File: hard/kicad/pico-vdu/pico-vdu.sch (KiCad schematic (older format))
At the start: 19 parts, among them M3 M3, U1 65C02, U10 74HC21, U11 74HC32, U2 74HC138, U3 74HC245, U4 74HC245, U5 74HC4040, U6 (74HC)4040, U7 6264/62256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

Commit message: some updates on pico-VDU
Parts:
- added U12: 74HC166, Package_DIP:DIP-16_W7.62mm_Socket, symbol 74xx:74LS166
- added U13: 74HC14, Package_DIP:DIP-14_W7.62mm_Socket, symbol 74xx:74HC14
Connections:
- net +5V: now also U12.1 (Ds), U12.16 (VCC), U12.9 (Clr), U13.14 (VCC)
- net DOT: now also U12.7 (Clk)
- net GND: now also U12.6 (CE), U12.8 (GND), U13.7 (GND)
- net VD0: now also U12.2 (A)
- net VD1: now also U12.3 (B)
- net VD2: now also U12.4 (C)
- net VD3: now also U12.5 (D)
- net VD4: now also U12.10 (E)
- net VD5: now also U12.11 (F)
- net VD6: now also U12.12 (G)
- net VD7: now also U12.14 (H)
- net ~CPU: now also U8.19 (CE)
- net ~LOST: now reaches U5.5 (Q3)
- no-connect marks 29 -> 28
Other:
- note added: "$0000-$1FFF\n\n$2000-$3FFF\n\n$4000-$5FFF\n\n$6000-$7FFF"
- moved on the sheet: R1, RN1, RN2, RN3, U11A, U11B, U11C, U11D, U7, U8, U9A

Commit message: remove stand and new tracks on pico-VDU
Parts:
- removed M3: M3, MountingHole:MountingHole_3.2mm_M3_DIN965_Pad, symbol Mechanical:MountingHole_Pad
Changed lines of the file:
@@
-	1    0    0    -1
-$EndComp
-$Comp
-L Mechanical:MountingHole_Pad M3
-U 1 1 663ED7C2
-P 1300 5650
-F 0 "M3" H 1400 5699 50  0000 L CNN
-F 1 "M3" H 1400 5608 50  0000 L CNN
-F 2 "MountingHole:MountingHole_3.2mm_M3_DIN965_Pad" H 1300 5650 50  0001 C CNN
-F 3 "~" H 1300 5650 50  0001 C CNN
-	1    1300 5650
 	1    0    0    -1
 $EndComp
@@
 	700  5750 1000 5750
 Connection ~ 1000 5750
-Wire Wire Line
-	1000 5750 1300 5750
 $Comp
 L power:GND #PWR0117

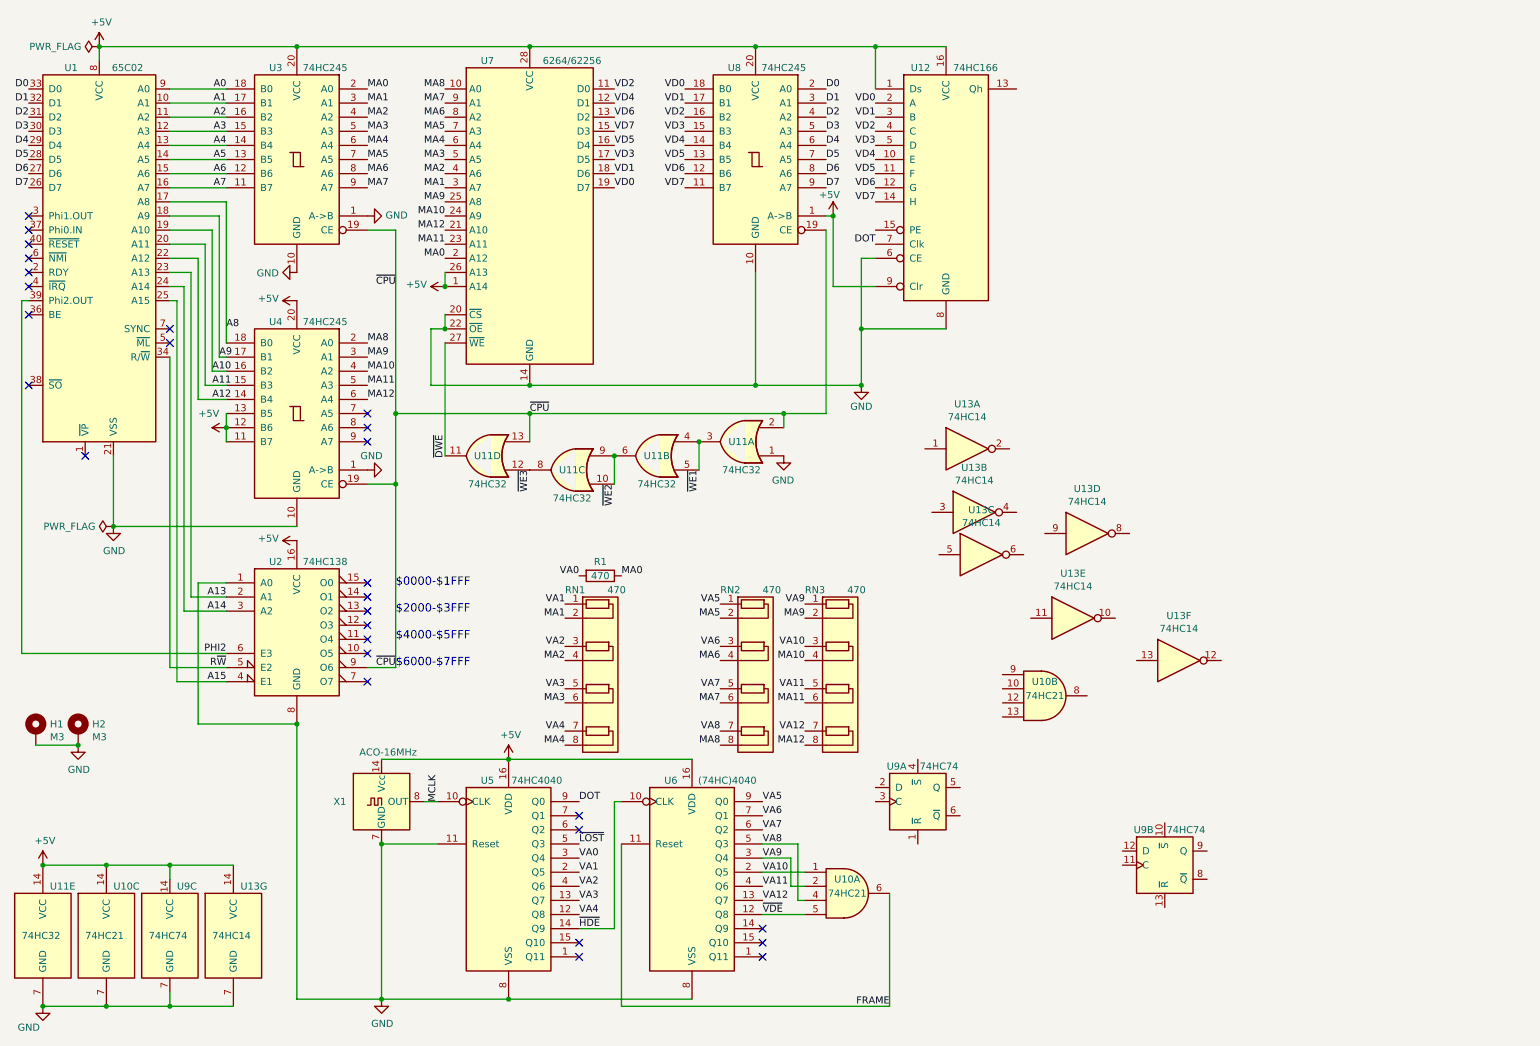
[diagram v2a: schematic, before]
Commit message: all addresses and thicker RCs
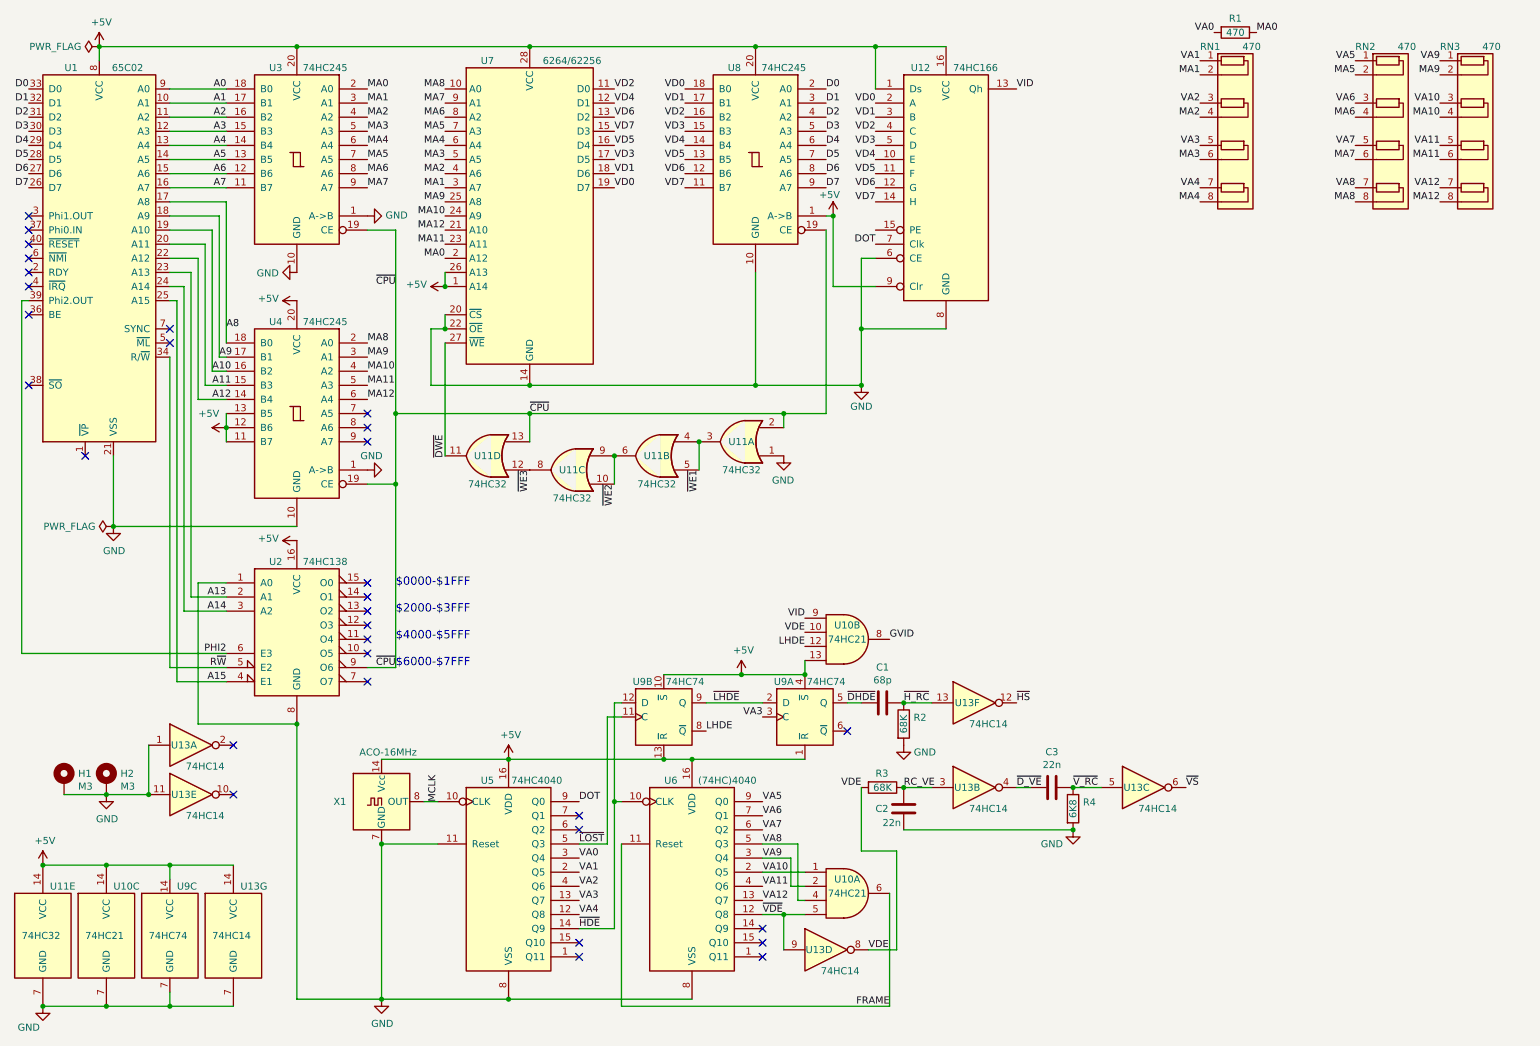
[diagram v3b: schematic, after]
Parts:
- added C1: 68p, Capacitor_THT:C_Disc_D3.8mm_W2.6mm_P2.50mm, symbol Device:C
- added C2, C3: 22n, Capacitor_THT:C_Rect_L7.2mm_W2.5mm_P5.00mm_FKS2_FKP2_MKS2_MKP2, symbol Device:C
- added R2, R3: 68K, Resistor_THT:R_Axial_DIN0207_L6.3mm_D2.5mm_P2.54mm_Vertical, symbol Device:R
- added R4: 6K8, Resistor_THT:R_Axial_DIN0207_L6.3mm_D2.5mm_P2.54mm_Vertical, symbol Device:R
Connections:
- net +5V: now also U10.13, U9.1 (~R), U9.10 (~S), U9.13 (~R), U9.4 (~S)
- net GND: now also U13.1, U13.11, C2.1, R2.2, R4.2
- net VA3: now also U9.3 (C)
- net ~HDE: now also U9.12 (D)
- net ~LOST: now also U9.11 (C)
- net ~VDE: now also U13.9
- net VDE: now reaches U10.10
- net VDE: now also U13.8, R3.2
- net LHDE: now reaches U10.12
- net LHDE: now also U9.8 (~Q)
- net GVID: now reaches U10.8
- net VID: now reaches U10.9
- net VID: now also U12.13 (Qh)
- net ~LHDE: now reaches U9.2 (D)
- net ~LHDE: now also U9.9 (Q)
- net ~DHDE: now reaches U9.5 (Q)
- net ~DHDE: now also C1.2
- net RC_VE: now reaches U13.3
- net RC_VE: now also C2.2, R3.1
- net ~D_VE: now reaches U13.4
- net ~D_VE: now also C3.2
- net ~V_RC: now reaches U13.5
- net ~V_RC: now also C3.1, R4.1
- net ~VS: now reaches U13.6
- net ~HS: now reaches U13.12
- net ~H_RC: now reaches U13.13
- net ~H_RC: now also C1.1, R2.1
- no-connect marks 28 -> 31
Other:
- moved on the sheet: H1, H2, R1, RN1, RN2, RN3, U10B, U13A, U13B, U13C, U13D, U13E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

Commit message: generate shift load
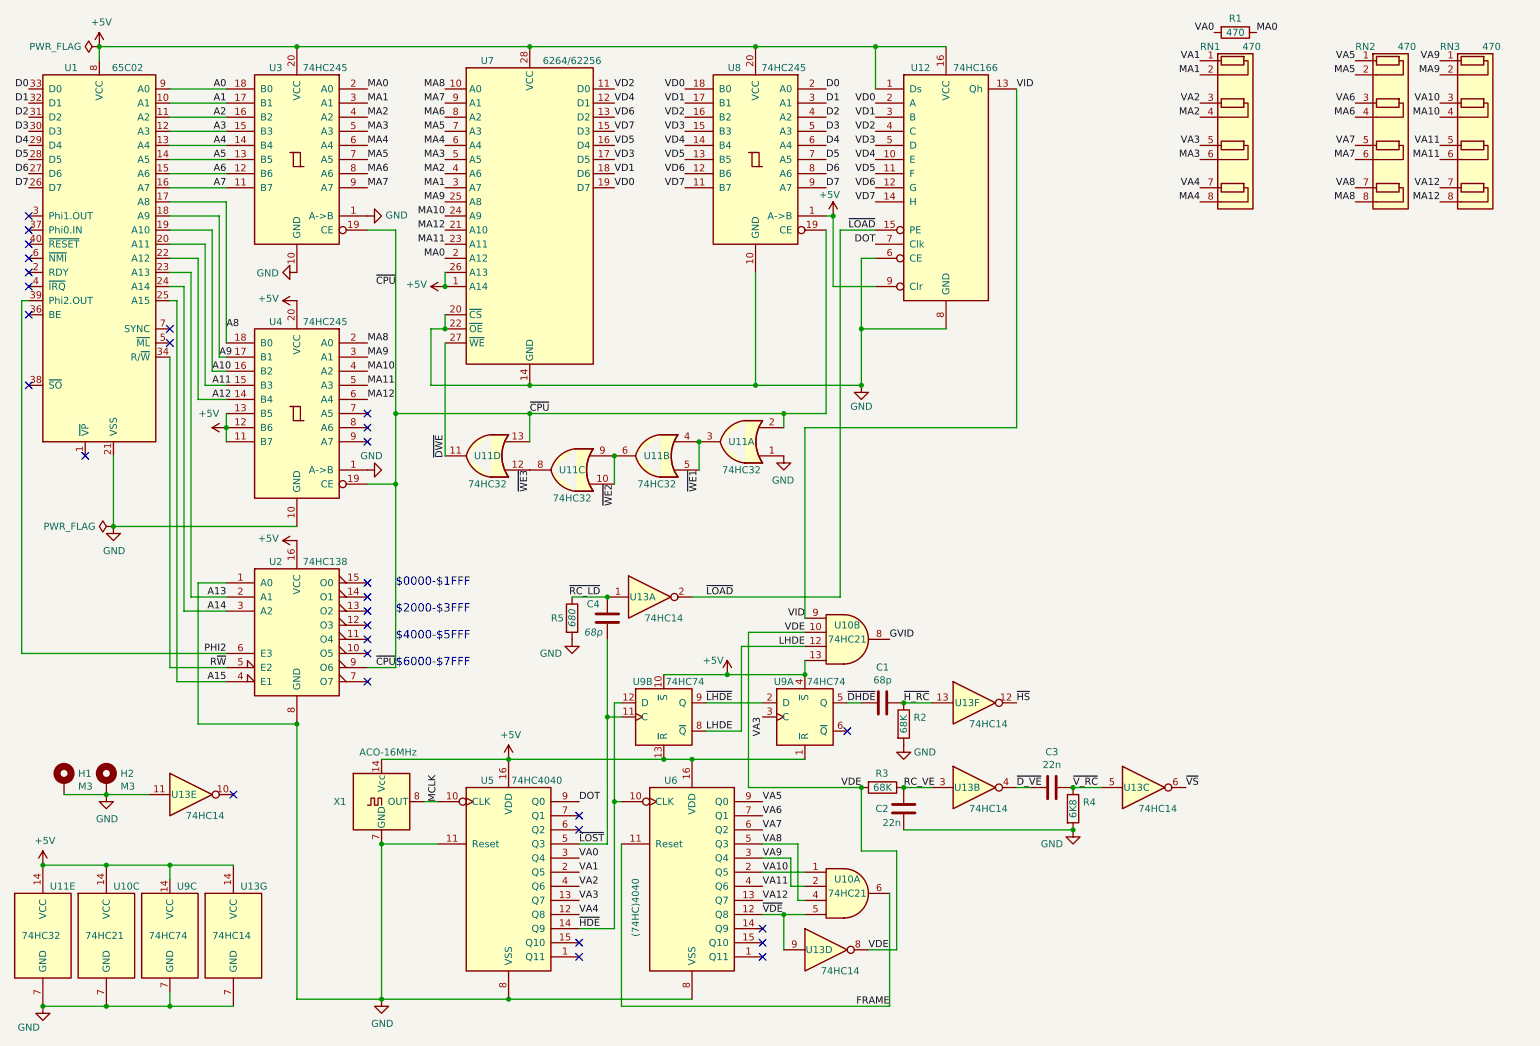
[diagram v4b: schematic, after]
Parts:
- added C4: 68p, Capacitor_THT:C_Disc_D3.8mm_W2.6mm_P2.50mm, symbol Device:C
- added R5: 680, Resistor_THT:R_Axial_DIN0207_L6.3mm_D2.5mm_P2.54mm_Vertical, symbol Device:R
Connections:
- net GND: now also R5.2; no longer U13.1
- net ~LOST: now also C4.1
- net ~LOAD: now reaches U12.15 (PE)
- net ~LOAD: now also U13.2
- new net ~RC_LD: C4.2, R5.1, U13.1
- no-connect marks 31 -> 30
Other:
- moved on the sheet: U13A
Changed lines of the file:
@@
 P 5350 6650
 F 0 "U6" H 5200 7300 50  0000 C CNN
-F 1 "(74HC)4040" H 5600 7300 50  0000 C CNN
+F 1 "(74HC)4040" V 4950 6400 50  0000 C CNN
 F 2 "Package_DIP:DIP-16_W7.62mm_Socket" H 5350 6650 50  0001 C CNN
 F 3 "http://www.intersil.com/content/dam/Intersil/documents/cd40/cd4020bms-24bms-40bms.pdf" H 5350 6650 50  0001 C CNN
@@
 L 74xx:74HC14 U13
 U 1 1 6631D2B2
-P 1800 5750
-F 0 "U13" H 1750 5750 50  0000 C CNN
-F 1 "74HC14" H 1900 5600 50  0000 C CNN
-F 2 "Package_DIP:DIP-14_W7.62mm_Socket" H 1800 5750 50  0001 C CNN
-F 3 "http://www.ti.com/lit/gpn/sn74HC14" H 1800 5750 50  0001 C CNN
-	1    1800 5750
+P 5050 4700
+F 0 "U13" H 5000 4700 50  0000 C CNN
+F 1 "74HC14" H 5150 4550 50  0000 C CNN
+F 2 "Package_DIP:DIP-14_W7.62mm_Socket" H 5050 4700 50  0001 C CNN
+F 3 "http://www.ti.com/lit/gpn/sn74HC14" H 5050 4700 50  0001 C CNN
+	1    5050 4700
 	1    0    0    -1
 $EndComp
@@
 	2100 7600 1650 7600
 Connection ~ 1650 7600
-Wire Wire Line
-	5450 5450 5850 5450
-Text Label 5500 5450 0    50   ~ 0
+Text Label 5450 5450 0    50   ~ 0
 ~LHDE
 Wire Wire Line
@@
 	4750 5550 4850 5550
 Wire Wire Line
-	5150 5250 5700 5250
+	5150 5250 5600 5250
 $Comp
 L power:+5V #PWR0118
 U 1 1 660A2824
-P 5700 5250
-F 0 "#PWR0118" H 5700 5100 50  0001 C CNN
-F 1 "+5V" H 5715 5423 50  0000 C CNN
-F 2 "" H 5700 5250 50  0001 C CNN
-F 3 "" H 5700 5250 50  0001 C CNN
-	1    5700 5250
-	1    0    0    -1
-$EndComp
-Connection ~ 5700 5250
-Wire Wire Line
-	5700 5250 6150 5250
-Text Label 5850 5550 2    50   ~ 0
+P 5600 5250
+F 0 "#PWR0118" H 5600 5100 50  0001 C CNN
+F 1 "+5V" H 5500 5350 50  0000 C CNN
+F 2 "" H 5600 5250 50  0001 C CNN
+F 3 "" H 5600 5250 50  0001 C CNN
+	1    5600 5250
+	1    0    0    -1
+$EndComp
+Connection ~ 5600 5250
+Wire Wire Line
+	5600 5250 6150 5250
+Text Label 5850 5550 3    50   ~ 0
 VA3
 Text Label 6450 5450 0    50   ~ 0
@@
 	6550 6500 6550 6050
 Wire Wire Line
-	1500 5750 1500 6100
-Wire Wire Line
 	1200 6100 1500 6100
-Connection ~ 1500 6100
-NoConn ~ 2100 5750
 NoConn ~ 2100 6100
+$Comp
+L Device:C C4
+U 1 1 660686A4
+P 4750 4850
+F 0 "C4" H 4850 4750 50  0000 C CNN
+F 1 "68p" H 4850 4950 50  0000 C CIN
+F 2 "Capacitor_THT:C_Disc_D3.8mm_W2.6mm_P2.50mm" H 4788 4700 50  0001 C CNN
+F 3 "~" H 4750 4850 50  0001 C CNN
+	1    4750 4850
+	-1   0    0    1
+$EndComp
+$Comp
+L Device:R R5
+U 1 1 6606AB4D
+P 4500 4850
+F 0 "R5" H 4350 4850 50  0000 L CNN
+F 1 "680" V 4500 4850 50  0000 C CIN
+F 2 "Resistor_THT:R_Axial_DIN0207_L6.3mm_D2.5mm_P2.54mm_Vertical" V 4430 4850 50  0001 C CNN
+F 3 "~" H 4500 4850 50  0001 C CNN
+	1    4500 4850
+	1    0    0    -1
+$EndComp
+$Comp
+L power:GND #PWR0121
+U 1 1 6606CAFB
+P 4500 5000
+F 0 "#PWR0121" H 4500 4750 50  0001 C CNN
+F 1 "GND" H 4350 4900 50  0000 C CNN
+F 2 "" H 4500 5000 50  0001 C CNN
+F 3 "" H 4500 5000 50  0001 C CNN
+	1    4500 5000
+	1    0    0    -1
+$EndComp
+Wire Wire Line
+	4750 5550 4750 5000
+Connection ~ 4750 5550
+Wire Wire Line
+	4500 4700 4750 4700
+Connection ~ 4750 4700
+Text Label 4700 4700 2    50   ~ 0
+~RC_LD
+Text Label 5450 4700 0    50   ~ 0
+~LOAD
+Text Label 6650 2100 2    50   ~ 0
+~LOAD
+Wire Wire Line
+	6150 4850 6150 3500
+Wire Wire Line
+	6150 3500 7650 3500
+Wire Wire Line
+	7650 3500 7650 1100
+Wire Wire Line
+	5450 5450 5850 5450
+Wire Wire Line
+	5450 5650 5700 5650
+Wire Wire Line
+	5700 5650 5700 5050
+Wire Wire Line
+	5700 5050 6150 5050
+Wire Wire Line
+	6550 6050 5750 6050
+Wire Wire Line
+	5750 6050 5750 4950
+Wire Wire Line
+	5750 4950 6150 4950
+Connection ~ 6550 6050
+Wire Wire Line
+	6650 2100 6400 2100
+Wire Wire Line
+	6400 2100 6400 4700
+Wire Wire Line
+	5350 4700 6400 4700
 $EndSCHEMATC

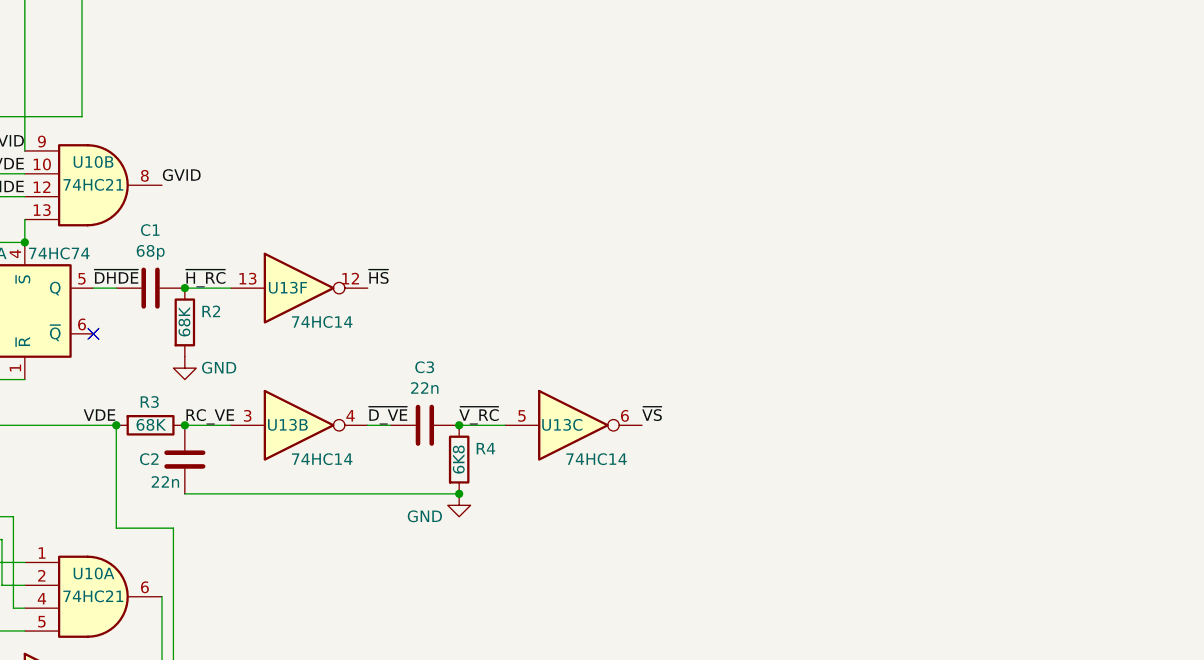
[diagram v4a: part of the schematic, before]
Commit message: analog section routed
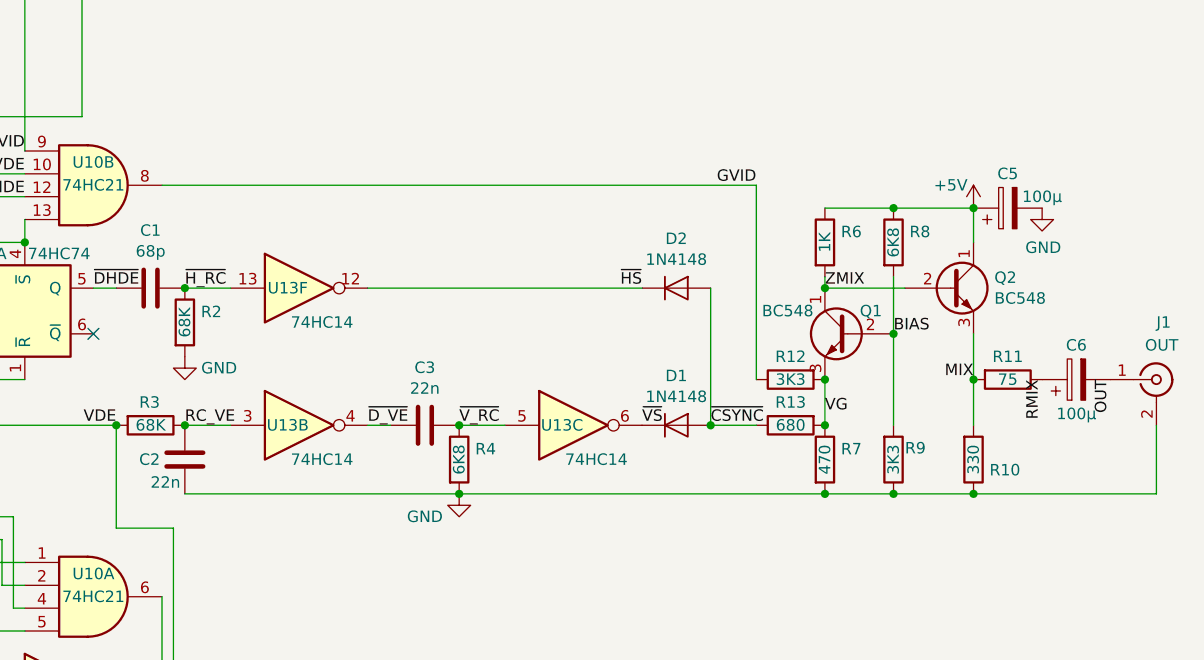
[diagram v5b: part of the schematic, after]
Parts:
- added C5, C6: 100µ, Capacitor_THT:CP_Radial_D4.0mm_P1.50mm, symbol Device:CP
- added D1, D2: 1N4148, Diode_THT:D_DO-35_SOD27_P2.54mm_Vertical_AnodeUp, symbol Diode:1N4148
- added J1: OUT, Connector_PinSocket_2.54mm:PinSocket_1x02_P2.54mm_Horizontal, symbol Connector:Conn_Coaxial
- added Q1, Q2: BC548, Package_TO_SOT_THT:TO-92_Inline, symbol Transistor_BJT:BC548
- added R10: 330, Resistor_THT:R_Axial_DIN0207_L6.3mm_D2.5mm_P2.54mm_Vertical, symbol Device:R
- added R11: 75, Resistor_THT:R_Axial_DIN0207_L6.3mm_D2.5mm_P2.54mm_Vertical, symbol Device:R
- added R12, R9: 3K3, Resistor_THT:R_Axial_DIN0207_L6.3mm_D2.5mm_P2.54mm_Vertical, symbol Device:R
- added R13: 680, Resistor_THT:R_Axial_DIN0207_L6.3mm_D2.5mm_P2.54mm_Vertical, symbol Device:R
- added R6: 1K, Resistor_THT:R_Axial_DIN0207_L6.3mm_D2.5mm_P2.54mm_Vertical, symbol Device:R
- added R7: 470, Resistor_THT:R_Axial_DIN0207_L6.3mm_D2.5mm_P2.54mm_Vertical, symbol Device:R
- added R8: 6K8, Resistor_THT:R_Axial_DIN0207_L6.3mm_D2.5mm_P2.54mm_Vertical, symbol Device:R
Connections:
- net +5V: now also C5.1, Q2.1 (C), R6.1, R8.1
- net GND: now also C5.2, J1.2 (Ext), R10.1, R7.2, R9.1
- net GVID: now also R12.1
- net ~HS: now also D2.1 (K)
- net ~VS: now also D1.1 (K)
- new net BIAS: Q1.2 (B), R8.2, R9.2
- new net MIX: Q2.3 (E), R10.2, R11.2
- new net OUT: C6.2, J1.1 (In)
- new net RMIX: C6.1, R11.1
- new net VG: Q1.3 (E), R12.2, R13.2, R7.1
- new net ZMIX: Q1.1 (C), Q2.2 (B), R6.2
- new net ~CSYNC: D1.2 (A), D2.2 (A), R13.1
